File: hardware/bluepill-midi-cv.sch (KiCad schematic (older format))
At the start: 2 parts

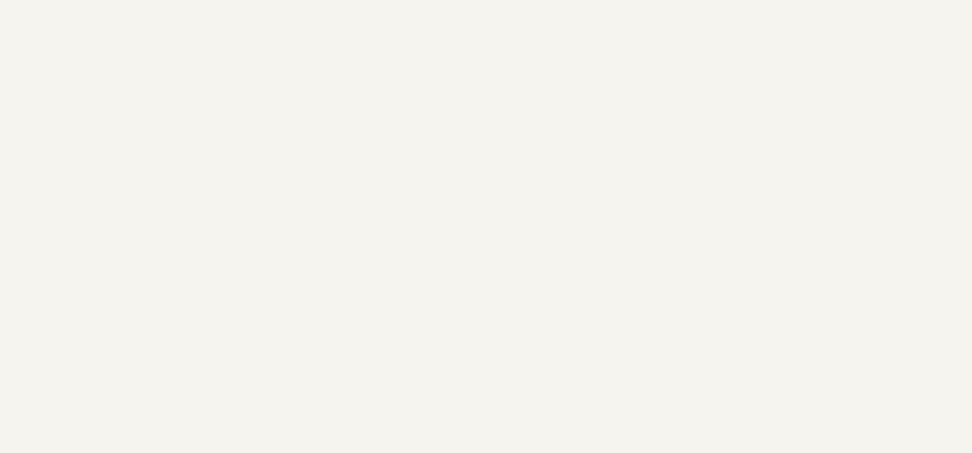
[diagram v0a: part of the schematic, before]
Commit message: add power connector and filtering for +/- 12v and 5v
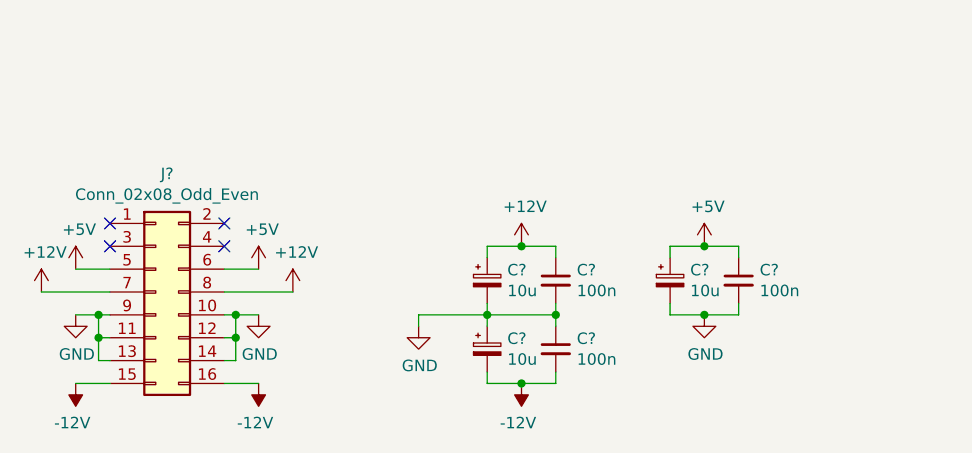
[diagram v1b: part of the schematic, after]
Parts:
- added C? (x3): 10u, symbol Device:CP_Small
- added C? (x3): 100n, symbol Device:C_Small
- added J?: Conn_02x08_Odd_Even, symbol Connector_Generic:Conn_02x08_Odd_Even
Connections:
- new net +12V: C?.1, C?.1, J?.7 (Pin_7), J?.8 (Pin_8)
- new net +5V: C?.1, C?.1, J?.5 (Pin_5), J?.6 (Pin_6)
- new net -12V: C?.2, C?.2, J?.15 (Pin_15), J?.16 (Pin_16)
- new net GND: C?.1, C?.1, C?.2, C?.2, C?.2, C?.2, J?.10 (Pin_10), J?.11 (Pin_11), J?.12 (Pin_12), J?.13 (Pin_13), J?.14 (Pin_14), J?.9 (Pin_9)
- no-connect marks 0 -> 4

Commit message: replace bluepill with newer version
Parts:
- removed U?: BluePill, symbol bluepill-midi-cv-rescue:BluePill-patchut
- added U?: BluePill, symbol patchut:BluePill
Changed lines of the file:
@@
 NoConn ~ 1300 6400
-$Comp
-L bluepill-midi-cv-rescue:BluePill-patchut U?
-U 1 1 5EA729A0
-P 4300 3900
-F 0 "U?" H 4300 5215 50  0000 C CNN
-F 1 "BluePill" H 4300 5124 50  0000 C CNN
-F 2 "" H 4300 4550 50  0001 C CNN
-F 3 "" H 4300 4550 50  0001 C CNN
-	1    4300 3900
-	1    0    0    -1
-$EndComp
 $Comp
 L Device:CP_Small C?
@@
 Wire Wire Line
 	3900 6400 4050 6400
+$Comp
+L patchut:BluePill U?
+U 1 1 5ECD805D
+P 3750 3800
+F 0 "U?" H 3750 5115 50  0000 C CNN
+F 1 "BluePill" H 3750 5024 50  0000 C CNN
+F 2 "" H 3750 3200 50  0001 C CNN
+F 3 "" H 3750 3200 50  0001 C CNN
+	1    3750 3800
+	1    0    0    -1
+$EndComp
 $EndSCHEMATC
